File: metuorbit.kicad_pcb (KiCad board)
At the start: 2 copper layers, 110 x 110 mm, 6 parts, among them IC1 BLACKPILLF4, IC2 LoRa E220-900T30D, IC3 BNO055, IC4 NEO-M8N, IC5 BMP388, IC6 MicroSD_Reader

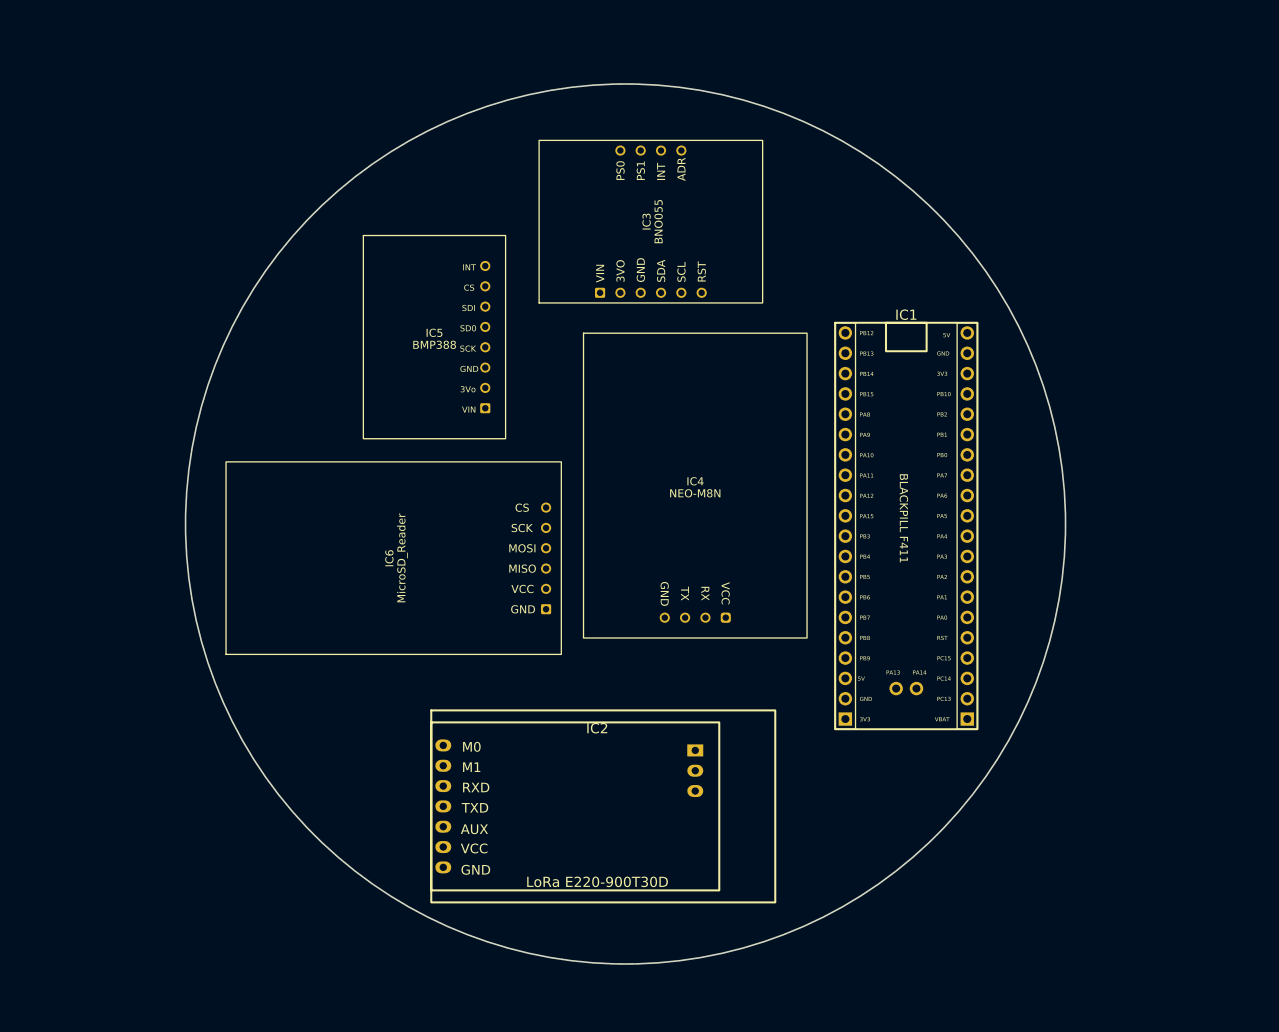
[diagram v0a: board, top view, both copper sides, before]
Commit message: Power regulators and output pins are added.
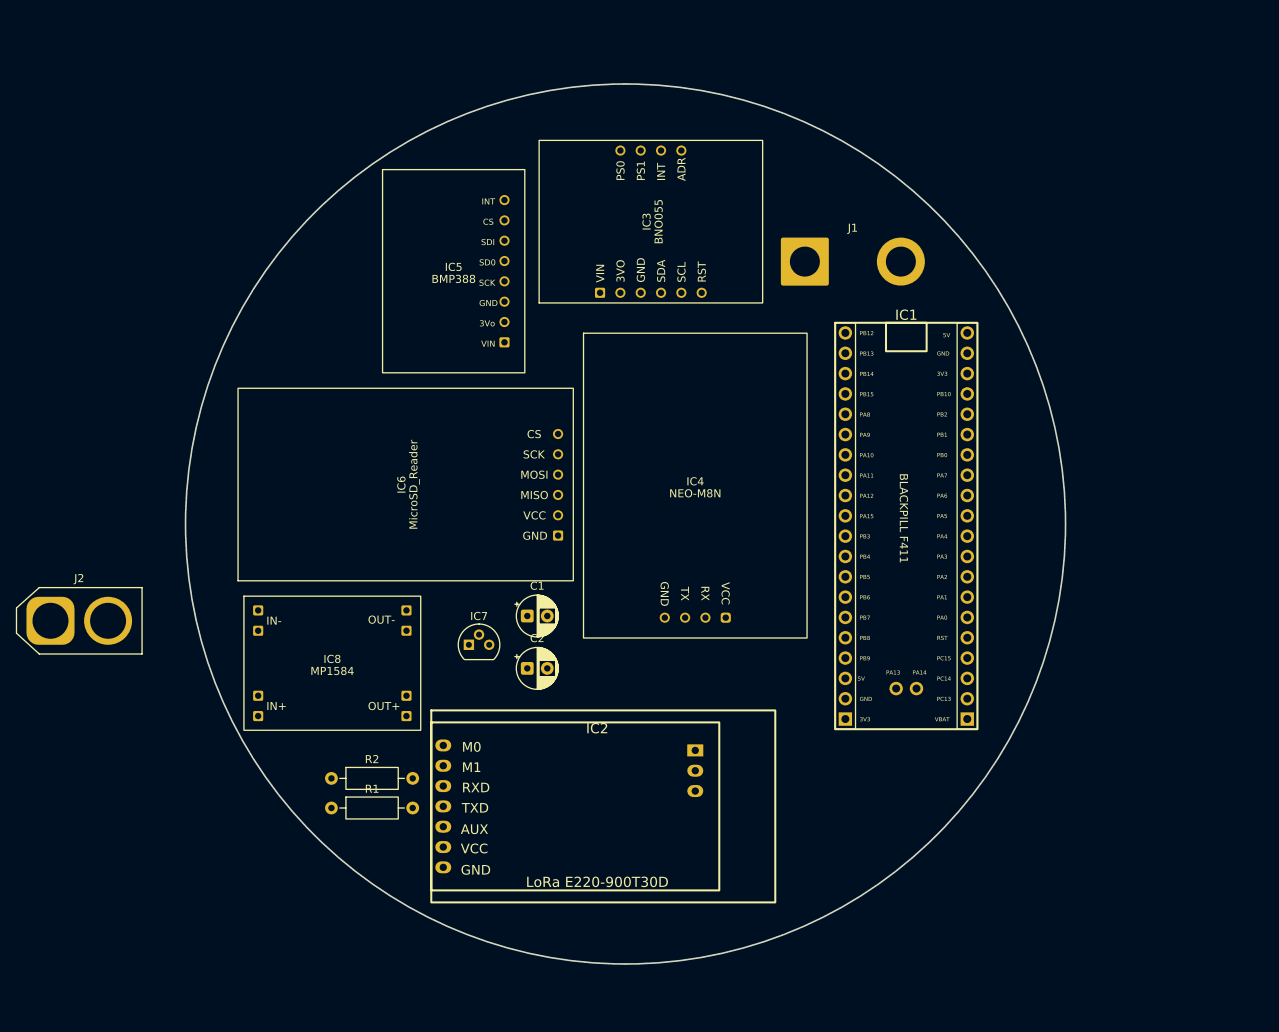
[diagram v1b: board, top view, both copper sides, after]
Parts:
- added C1: 10u, Capacitor_THT:CP_Radial_D5.0mm_P2.50mm, F.Cu at (193.0, 170.0)
- added C2: 10u, Capacitor_THT:CP_Radial_D5.0mm_P2.50mm, F.Cu at (193.0, 176.6)
- added IC7: HT7333, Package_TO_SOT_THT:TO-92, F.Cu at (185.7, 173.6)
- added IC8: MP1584, Boards:MP1584, F.Cu at (168.6, 175.9)
- added J1: BATT Output, Connector_Wire:SolderWire-4sqmm_1x02_P12mm_D3mm_OD6mm, F.Cu at (227.7, 125.7)
- added J2: BATT Input, Connector_AMASS:AMASS_XT60-F_1x02_P7.20mm_Vertical, F.Cu at (133.4, 170.6)
- added R1: 1k, Resistor_THT:R_Axial_DIN0207_L6.3mm_D2.5mm_P10.16mm_Horizontal, F.Cu at (168.5, 194.0)
- added R2: 1k, Resistor_THT:R_Axial_DIN0207_L6.3mm_D2.5mm_P10.16mm_Horizontal, F.Cu at (168.5, 190.3)
- moved IC6 9.32 mm to (177.8, 153.6)
- moved IC5 8.58 mm to (183.8, 126.9)
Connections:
- IC1 pad PA10: unconnected-(IC1-PadPA10) -> /LORA_TX
- IC1 pad PA9: unconnected-(IC1-PadPA9) -> /LORA_RX
- IC2 pad 1: unconnected-(IC2-M0-Pad1) -> /LORA_M0
- IC2 pad 2: unconnected-(IC2-M1-Pad2) -> /LORA_M1
- IC2 pad 3: unconnected-(IC2-RXD-Pad3) -> Net-(IC2-RXD)
- IC2 pad 4: unconnected-(IC2-TXD-Pad4) -> Net-(IC2-TXD)
- IC2 pad 6: unconnected-(IC2-VCC-Pad6) -> +5V
- IC2 pad 7: unconnected-(IC2-GND-Pad7) -> GND

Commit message: General layout in pcb is determined.
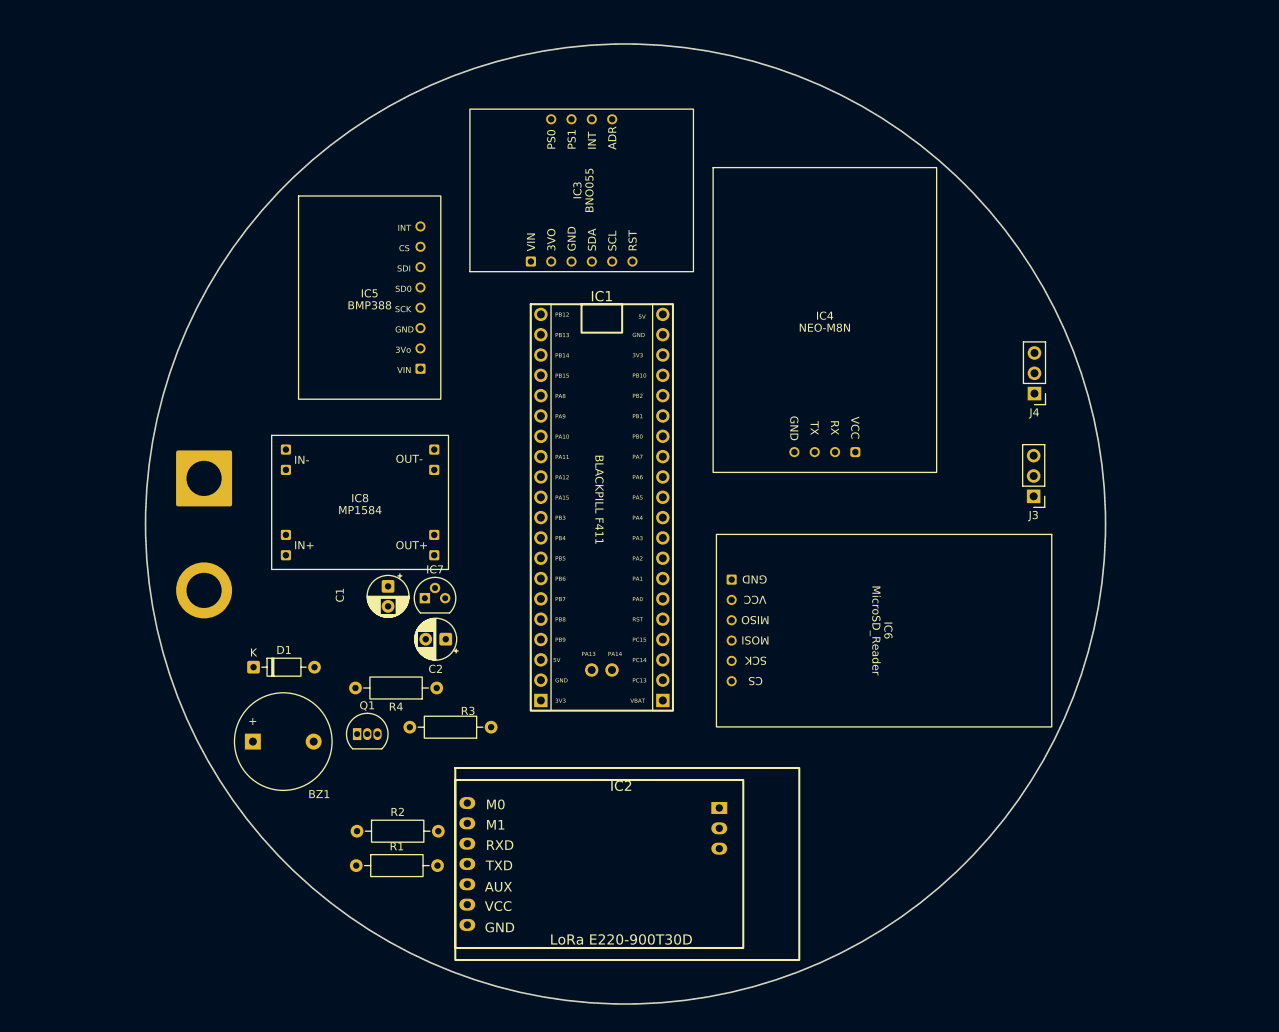
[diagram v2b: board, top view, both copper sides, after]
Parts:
- removed J1: BATT Output, Connector_Wire:SolderWire-4sqmm_1x02_P12mm_D3mm_OD6mm
- added BZ1: Buzzer, Buzzer_Beeper:Buzzer_12x9.5RM7.6, F.Cu at (158.7, 185.7)
- added D1: 1N4148, Diode_THT:D_DO-35_SOD27_P7.62mm_Horizontal, F.Cu at (158.8, 176.4)
- added J3: SERVO1, Connector_PinHeader_2.54mm:PinHeader_1x03_P2.54mm_Vertical, F.Cu at (256.3, 155.0)
- added J4: SERVO2, Connector_PinHeader_2.54mm:PinHeader_1x03_P2.54mm_Vertical, F.Cu at (256.4, 142.2)
- added Q1: 2N3904, Package_TO_SOT_THT:TO-92_Inline, F.Cu at (171.7, 184.8)
- added R3: 1k, Resistor_THT:R_Axial_DIN0207_L6.3mm_D2.5mm_P10.16mm_Horizontal, F.Cu at (188.5, 183.9)
- added R4: 10k, Resistor_THT:R_Axial_DIN0207_L6.3mm_D2.5mm_P10.16mm_Horizontal, F.Cu at (181.7, 179.0)
- J2: footprint Connector_AMASS:AMASS_XT60-F_1x02_P7.20mm_Vertical -> Connector_Wire:SolderWire-6sqmm_1x02_P14mm_D3.5mm_OD7mm; moved to B.Cu
- moved IC6 62.5 mm to (237.6, 171.8), turned to -90 degrees
- moved IC1 38.1 mm to (202.3, 157.7)
- moved IC4 26.3 mm to (230.2, 133.0)
- moved J2 26.2 mm to (152.6, 152.8), turned to -90 degrees
- moved IC8 20.4 mm to (172.1, 155.8)
- moved C1 17.8 mm to (175.6, 166.3), turned to -90 degrees
- moved IC5 11.0 mm to (173.3, 130.2)
- moved C2 10.8 mm to (182.8, 172.9), turned to 180 degrees
- moved IC3 9.49 mm to (199.8, 116.8)
- moved IC7 8.01 mm to (180.2, 167.8)
- moved R1 7.84 mm to (171.6, 201.2)
- moved IC2 7.80 mm to (185.5, 193.4)
- moved R2 7.33 mm to (171.7, 196.9)
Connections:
- IC1 pad 3V3_2: unconnected-(IC1-3V3-Pad3V3_2) -> +3V3
- IC1 pad PA0: unconnected-(IC1-PadPA0) -> /LORA_M0
- IC1 pad PA1: unconnected-(IC1-PadPA1) -> /LORA_M1
- IC1 pad PB0: unconnected-(IC1-PadPB0) -> /SERVO1
- IC1 pad PB1: unconnected-(IC1-PadPB1) -> /SERVO2
- IC1 pad PC13: unconnected-(IC1-PadPC13) -> /BUZZ
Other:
- board size 110 x 110 mm -> 120 x 120 mm

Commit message: Resistors are changed to SMD, Schematic is organized.
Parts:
- R1, R2, R3, R4: footprint Resistor_THT:R_Axial_DIN0207_L6.3mm_D2.5mm_P10.16mm_Horizontal -> Resistor_SMD:R_1206_3216Metric_Pad1.30x1.75mm_HandSolder
- moved R3 13.1 mm to (176.2, 179.2)
- moved R4 11.1 mm to (170.6, 179.2)
- moved R2 9.07 mm to (180.7, 198.5)
- moved R1 9.03 mm to (180.7, 201.0)
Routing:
- net +BATT: track 0.00 -> 14.6 mm
- net GND: track 0.00 -> 13.2 mm
- net Net-(IC2-TXD): track 0.00 -> 3.30 mm
- net Net-(IC2-RXD): track 0.00 -> 3.30 mm

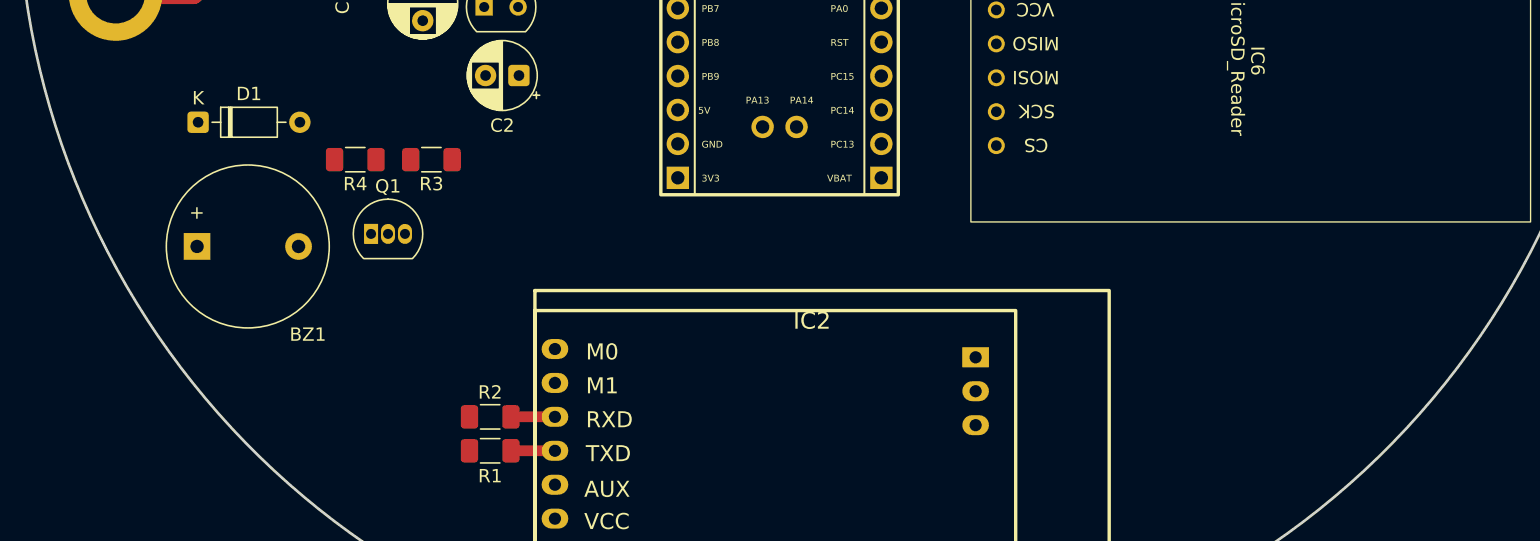
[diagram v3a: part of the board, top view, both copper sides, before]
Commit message: Resistive wire trigger is added.
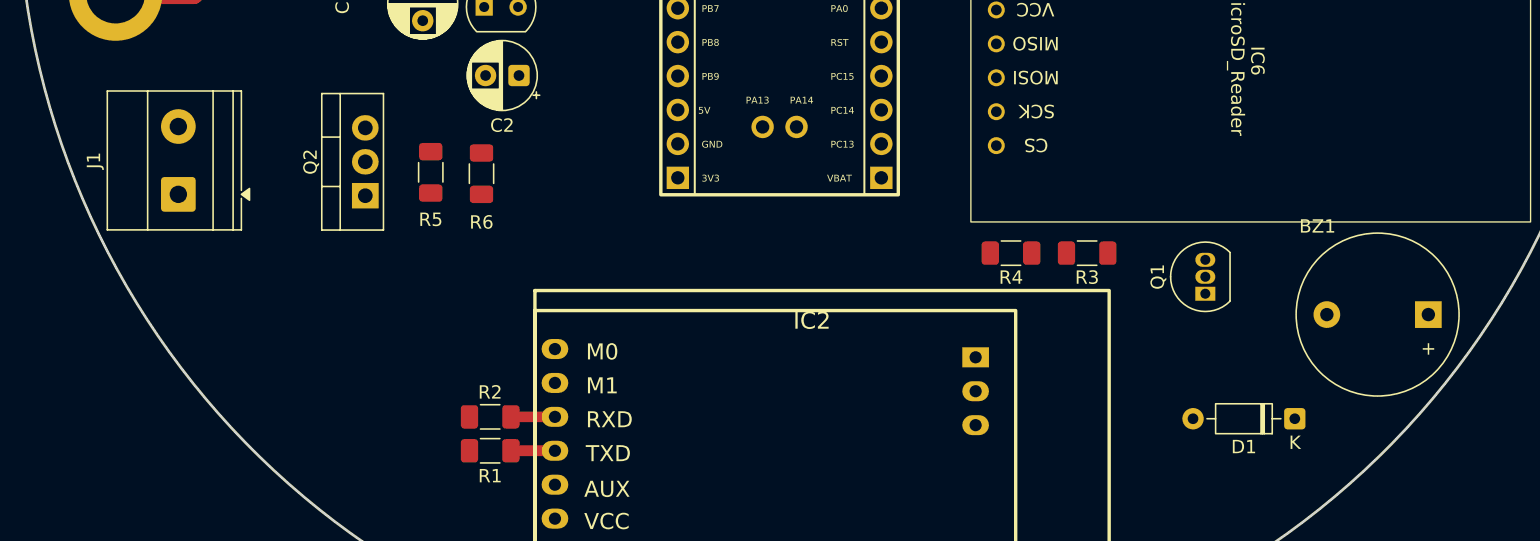
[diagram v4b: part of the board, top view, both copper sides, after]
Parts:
- added J1: Resistive Wire, TerminalBlock_Phoenix:TerminalBlock_Phoenix_MKDS-1,5-2-5.08_1x02_P5.08mm_Horizontal, F.Cu at (157.3, 181.8)
- added Q2: IRLZ44N, Package_TO_SOT_THT:TO-220-3_Vertical, F.Cu at (171.3, 181.9)
- added R5: 10k, Resistor_SMD:R_1206_3216Metric_Pad1.30x1.75mm_HandSolder, F.Cu at (176.2, 180.2)
- added R6: 220, Resistor_SMD:R_1206_3216Metric_Pad1.30x1.75mm_HandSolder, F.Cu at (180.0, 180.2)
- moved BZ1 92.3 mm to (250.9, 190.8), turned to 180 degrees
- moved D1 85.1 mm to (240.9, 198.6), turned to 180 degrees
- moved Q1 62.6 mm to (234.2, 189.2), turned to 90 degrees
- moved R3 49.6 mm to (225.3, 186.2)
- moved R4 49.6 mm to (219.7, 186.2)
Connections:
- IC1 pad PB2: unconnected-(IC1-PadPB2) -> /TRIG

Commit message: First design of PCB is done.
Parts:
- added C3: 470u, Capacitor_THT:CP_Radial_D5.0mm_P2.50mm, F.Cu at (157.6, 159.0)
- J2: moved to F.Cu
- moved R4 9.18 mm to (225.7, 193.1)
- moved IC2 5.89 mm to (179.9, 191.7)
- moved R1 5.89 mm to (175.0, 199.3)
- moved R2 5.89 mm to (175.0, 196.8)
- moved J1 5.72 mm to (157.8, 176.1), turned to -90 degrees
- moved D1 2.47 mm to (238.8, 199.9), turned to 90 degrees
- moved J2 2.20 mm to (151.2, 151.1)
- moved R3 1.06 mm to (225.7, 187.2), turned to 0 degrees
- moved Q2 0.72 mm to (171.3, 181.2)
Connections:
- IC1 pad PA10: /LORA_TX -> /LORA_RX
- IC1 pad PA9: /LORA_RX -> /LORA_TX
- IC1 pad PB2: /TRIG -> unconnected-(IC1-PadPB2)
- IC1 pad PB5: unconnected-(IC1-PadPB5) -> /TRIG
- IC4 pad 1: GND -> +3V3
- IC4 pad 2: /NEO_TX -> /NEO_RX
- IC4 pad 3: /NEO_RX -> /NEO_TX
- IC4 pad 4: +3V3 -> GND
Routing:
- net +5V: track 0.00 -> 207.4 mm
- net +3V3: track 0.00 -> 176.4 mm
- net /LORA_TX: track 0.00 -> 66.8 mm
- net /LORA_RX: track 0.00 -> 59.9 mm
- net /LORA_M1: track 0.00 -> 52.6 mm
- net /SERVO1: track 0.00 -> 50.0 mm
- net /SERVO2: track 0.00 -> 48.7 mm
- net /LORA_M0: track 0.00 -> 44.5 mm
- net /BMP_SDA: track 0.00 -> 43.2 mm
- net /BNO_SDA: track 0.00 -> 34.6 mm
- net /SD_MOSI: track 0.00 -> 33.9 mm
- net /NEO_RX: track 0.00 -> 27.0 mm
- net /TRIG: track 0.00 -> 24.2 mm, vias 0 -> 1
- net /SD_SCK: track 0.00 -> 24.0 mm
- net /SD_CS: track 0.00 -> 24.0 mm
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- added copper zone on B.Cu, net GND
- added copper zone on F.Cu, net GND

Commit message: PCB is reorganized. Some texts are added.
Checking the design is needed.
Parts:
- removed C3: 470u, Capacitor_THT:CP_Radial_D5.0mm_P2.50mm
- added C4: 470u, Capacitor_THT:CP_Radial_D8.0mm_P3.50mm, F.Cu at (184.6, 159.8)
- moved IC8 3.35 mm to (168.8, 155.8)
- moved R4 2.35 mm to (225.7, 190.8)
- moved R5 0.10 mm to (176.2, 180.2)
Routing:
- net GND: track 35.8 -> 10.2 mm, vias 2 -> 58
- net +BATT: track 36.2 -> 24.0 mm
- net +5V: track 207.4 -> 215.4 mm
- net Net-(Q1-B): track 13.2 -> 10.8 mm
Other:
- board text added: "+"
- board text added: "-"
- board text added: "METUORBIT Flight Control PCB v1.0"
- board text added: "by Ataberk ASLAN"

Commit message: LEDs for power lines are added. Some connections are adjusted.
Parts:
- added D2: LED, LED_SMD:LED_1206_3216Metric_Pad1.42x1.75mm_HandSolder, F.Cu at (160.3, 141.3)
- added D3: LED, LED_SMD:LED_1206_3216Metric_Pad1.42x1.75mm_HandSolder, F.Cu at (160.3, 136.1)
- added G***: LOGO, Logos:logo, B.Cu at (243.5, 156.2)
- added R7: 220, Resistor_SMD:R_1206_3216Metric_Pad1.30x1.75mm_HandSolder, F.Cu at (154.3, 141.3)
- added R8: 220, Resistor_SMD:R_1206_3216Metric_Pad1.30x1.75mm_HandSolder, F.Cu at (154.3, 136.2)
- moved C1 0.30 mm to (175.9, 166.3)
- moved C2 0.25 mm to (182.8, 172.7)
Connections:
- IC1 pad PB9: unconnected-(IC1-PadPB9) -> /BUZZ
- IC1 pad PC13: /BUZZ -> unconnected-(IC1-PadPC13)
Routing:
- net /BUZZ: track 18.0 -> 45.0 mm, vias 0 -> 1
- net +5V: track 215.4 -> 240.2 mm
- net +3V3: track 176.4 -> 195.3 mm
- net Net-(D3-K): track 0.00 -> 2.96 mm
- net Net-(D2-K): track 0.00 -> 2.92 mm
- net /SD_MISO: track 23.0 -> 22.3 mm
- net GND: track 10.2 -> 9.65 mm, vias 58 -> 95

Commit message: Traces and connecters are adjusted for ESC.
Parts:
- removed J4: SERVO2, Connector_PinHeader_2.54mm:PinHeader_1x03_P2.54mm_Vertical
- moved J3 6.54 mm to (261.5, 159.0)
- moved G*** 3.01 mm to (243.5, 159.3)
- moved J2 0.40 mm to (151.2, 151.5)
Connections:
- IC1 pad PB1: /SERVO2 -> unconnected-(IC1-PadPB1)
- IC1 pad PB8: unconnected-(IC1-PadPB8) -> /LORA_AUX
- IC2 pad 5: unconnected-(IC2-AUX-Pad5) -> /LORA_AUX
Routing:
- net /SERVO2: track 48.7 -> 0.00 mm
- net /LORA_AUX: track 0.00 -> 47.4 mm
- net +5V: track 240.2 -> 228.4 mm
- net /SERVO1: track 50.0 -> 55.3 mm
- net /LORA_M0: track 44.5 -> 47.2 mm
- net /LORA_RX: track 59.9 -> 62.2 mm
- net /SD_CS: track 24.0 -> 24.9 mm
- net /BNO_SDA: track 34.6 -> 35.4 mm
- net /BNO_SCL: track 18.5 -> 19.2 mm
- net /SD_SCK: track 24.0 -> 24.7 mm
- net /BUZZ: track 45.0 -> 44.7 mm, vias 1 -> 2
- net GND: vias 95 -> 123
